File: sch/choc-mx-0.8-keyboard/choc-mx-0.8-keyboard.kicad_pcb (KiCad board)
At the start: 2 copper layers, 166 x 95 mm, 81 parts, among them SW1 SW_Push, SW10 SW_Push, SW11 SW_Push, SW12 SW_Push, SW13 SW_Push, SW14 SW_Push, SW15 SW_Push, SW16 SW_Push, SW17 SW_Push, SW18 SW_Push, SW19 SW_Push, SW2 SW_Push, SW20 SW_Push, SW21 SW_Push, SW22 SW_Push, SW23 SW_Push, SW24 SW_Push, SW25 SW_Push, SW26 SW_Push, SW27 SW_Push, SW28 SW_Push, SW29 SW_Push, SW3 SW_Push, SW30 SW_Push, SW31 SW_Push, SW32 SW_Push, SW33 SW_Push, SW34 SW_Push, SW35 SW_Push, SW36 SW_Push, SW37 SW_Push, SW38 SW_Push, SW39 SW_Push, SW4 SW_Push, SW40 SW_Push, SW5 SW_Push, SW6 SW_Push, SW7 SW_Push, SW8 SW_Push, SW9 SW_Push, U1 Pico

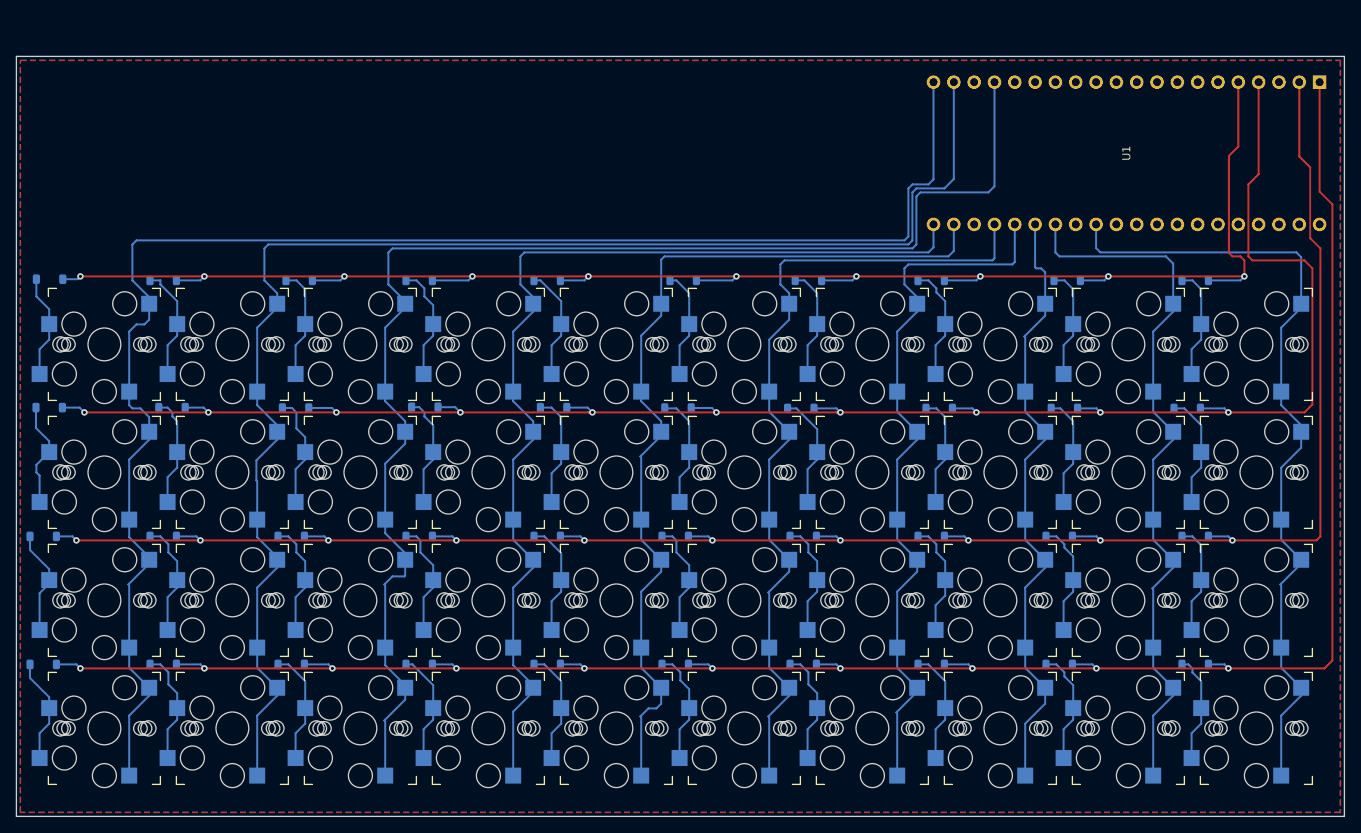
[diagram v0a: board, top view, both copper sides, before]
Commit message: AE-RP2040も使えるようにしました。
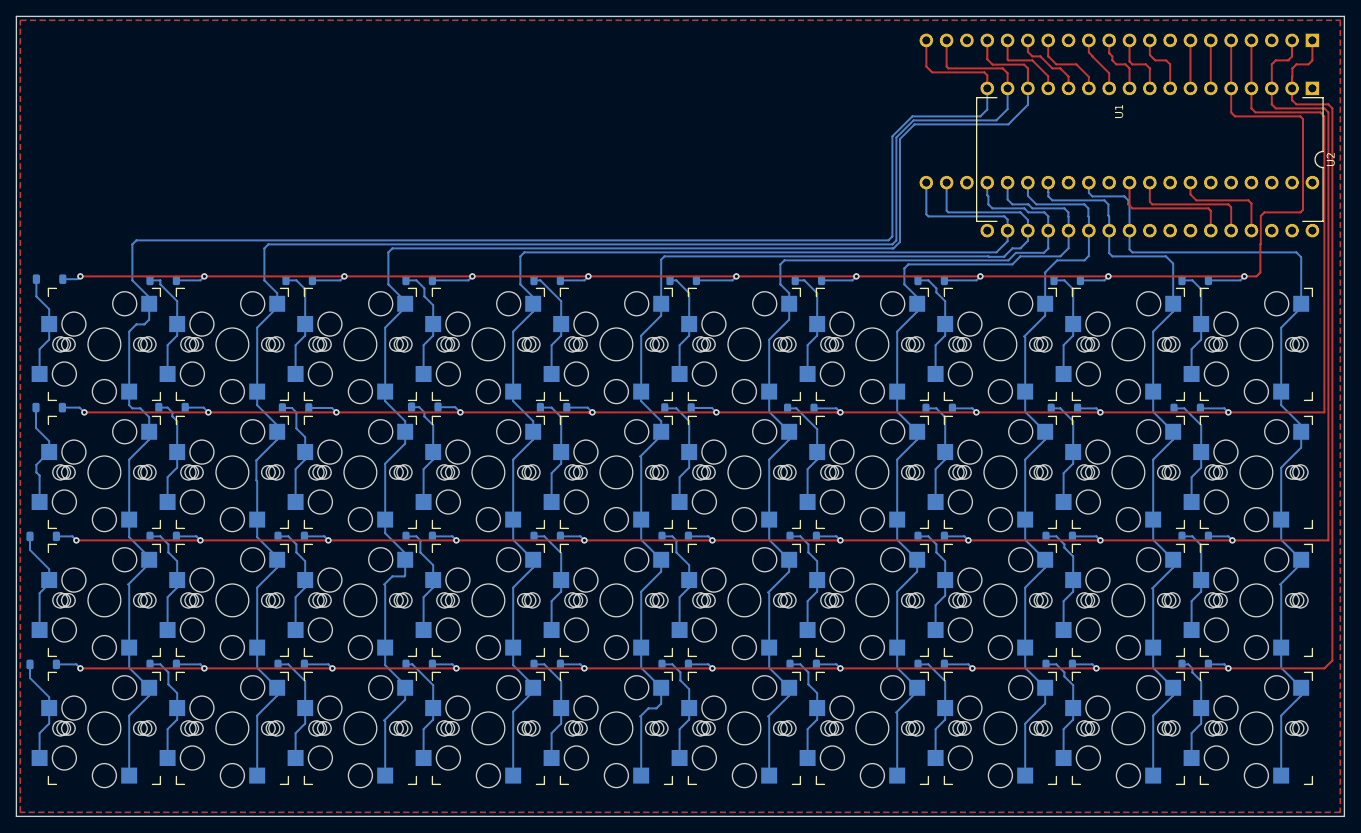
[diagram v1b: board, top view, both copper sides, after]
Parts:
- added U2: ~, ae-rp2040:AE-RP2040, F.Cu at (197.0, 44.0)
- moved U1 5.30 mm to (172.9, 46.9)
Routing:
- net /GPIO16: track 127.8 -> 151.6 mm
- net /GPIO17: track 112.8 -> 136.1 mm
- net /GPIO3: track 213.7 -> 232.1 mm
- net /GPIO14: track 179.3 -> 197.3 mm
- net /GPIO18: track 103.1 -> 121.0 mm
- net /GPIO15: track 194.9 -> 212.6 mm
- net /GPIO19: track 90.2 -> 107.8 mm
- net /GPIO26: track 0.00 -> 15.8 mm
- net /GPIO27: track 0.00 -> 15.8 mm
- net /GPIO20: track 77.1 -> 92.4 mm
- net /GPIO1: track 245.7 -> 259.5 mm
- net /GPIO28: track 0.00 -> 13.0 mm
- net /GPIO13: track 170.3 -> 182.1 mm
- net /GPIO0: track 262.9 -> 273.9 mm
- net /GPIO12: track 0.00 -> 9.86 mm
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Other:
- board size 166 x 95 mm -> 166 x 100 mm
